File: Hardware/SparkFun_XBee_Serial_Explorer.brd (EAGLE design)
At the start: 57.1 x 48.3 mm, 51 parts, among them Q1 MBT2222, U1 MAX232SOIC16, U2 XBEE-1B3, U3 LM117

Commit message: Final QC checklist and changes for testbed
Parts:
- moved TP2 1.27 mm to (24.1, 16.5)
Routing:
- net RS232-CTS: track 24.8 -> 26.0 mm
- net RTS: track 42.0 -> 42.5 mm
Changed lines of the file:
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@@
 <layer number="47" name="Measures" color="7" fill="1" visible="no" active="yes"/>
 <layer number="48" name="Document" color="7" fill="1" visible="no" active="yes"/>
-<layer number="49" name="Reference" color="7" fill="1" visible="yes" active="yes"/>
+<layer number="49" name="Reference" color="7" fill="1" visible="no" active="yes"/>
 <layer number="50" name="dxf" color="7" fill="1" visible="no" active="yes"/>
 <layer number="51" name="tDocu" color="6" fill="1" visible="yes" active="yes"/>
@@
 <element name="LOGO3" library="SparkFun-Aesthetics" package="SFE_LOGO_FLAME_.1" value="SFE_LOGO_FLAME.1_INCH" x="6.604" y="1.3208"/>
 <element name="TP1" library="SparkFun-Passives" package="TP_15TH" value="TEST-POINTTP_15TH_THRU" x="25.4" y="19.05"/>
-<element name="TP2" library="SparkFun-Passives" package="TP_15TH" value="TEST-POINTTP_15TH_THRU" x="24.13" y="17.78"/>
+<element name="TP2" library="SparkFun-Passives" package="TP_15TH" value="TEST-POINTTP_15TH_THRU" x="24.13" y="16.51"/>
 <element name="TP3" library="SparkFun-Passives" package="TP_15TH" value="TEST-POINTTP_15TH_THRU" x="8.89" y="34.29"/>
 <element name="TP4" library="SparkFun-Passives" package="TP_15TH" value="TEST-POINTTP_15TH_THRU" x="21.59" y="34.29"/>
@@
 <wire x1="10.82" y1="15.94" x2="6.92" y2="15.94" width="0.254" layer="1"/>
 <wire x1="6.92" y1="15.94" x2="5.08" y2="17.78" width="0.254" layer="1"/>
-<wire x1="26.67" y1="15.875" x2="6.985" y2="15.875" width="0.254" layer="16"/>
-<wire x1="6.985" y1="15.875" x2="5.08" y2="17.78" width="0.254" layer="16"/>
+<wire x1="7.62" y1="15.24" x2="5.08" y2="17.78" width="0.254" layer="16"/>
 <wire x1="27.051" y1="16.256" x2="26.67" y2="15.875" width="0.254" layer="1"/>
+<wire x1="7.62" y1="15.24" x2="26.035" y2="15.24" width="0.254" layer="16"/>
+<wire x1="26.035" y1="15.24" x2="26.67" y2="15.875" width="0.254" layer="16"/>
 </signal>
 <signal name="DIO3">
@@
 <wire x1="24.765" y1="22.6" x2="24.765" y2="20.32" width="0.254" layer="1"/>
 <wire x1="24.765" y1="20.32" x2="24.13" y2="19.685" width="0.254" layer="1"/>
-<wire x1="24.13" y1="19.685" x2="24.13" y2="17.78" width="0.254" layer="1"/>
+<wire x1="24.13" y1="19.685" x2="24.13" y2="16.51" width="0.254" layer="1"/>
 </signal>
 <signal name="RS232-DTR">

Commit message: moved fids slightly
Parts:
- moved U$16 2.84 mm to (54.6, 7.62)
- moved U$7 2.84 mm to (2.54, 40.6)

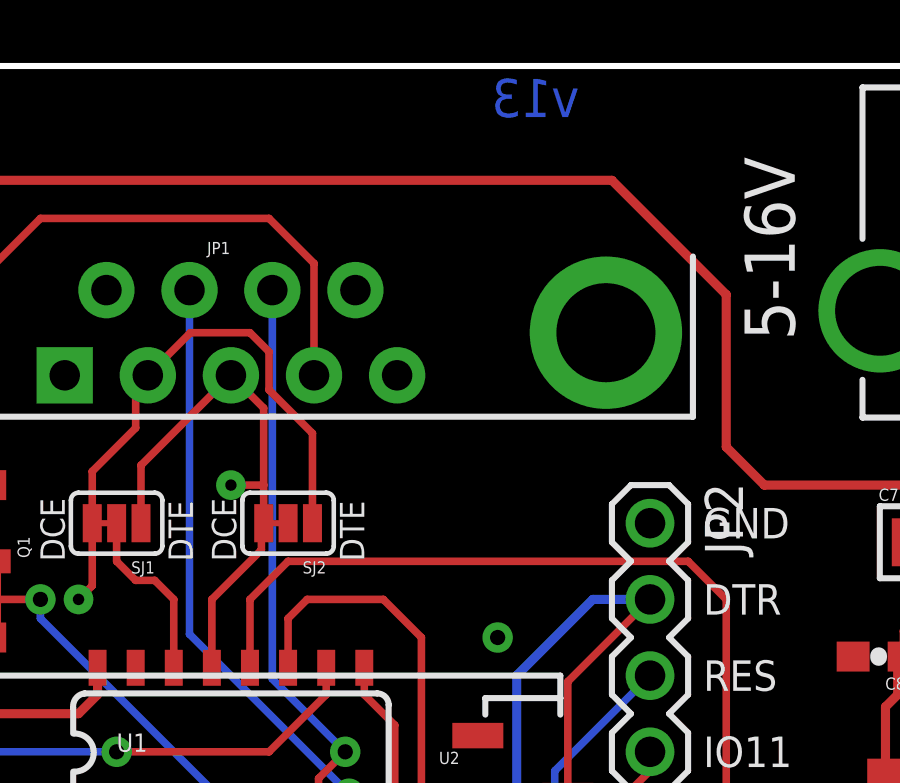
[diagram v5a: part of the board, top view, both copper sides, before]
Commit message: Fixing jumper trace, updating version number
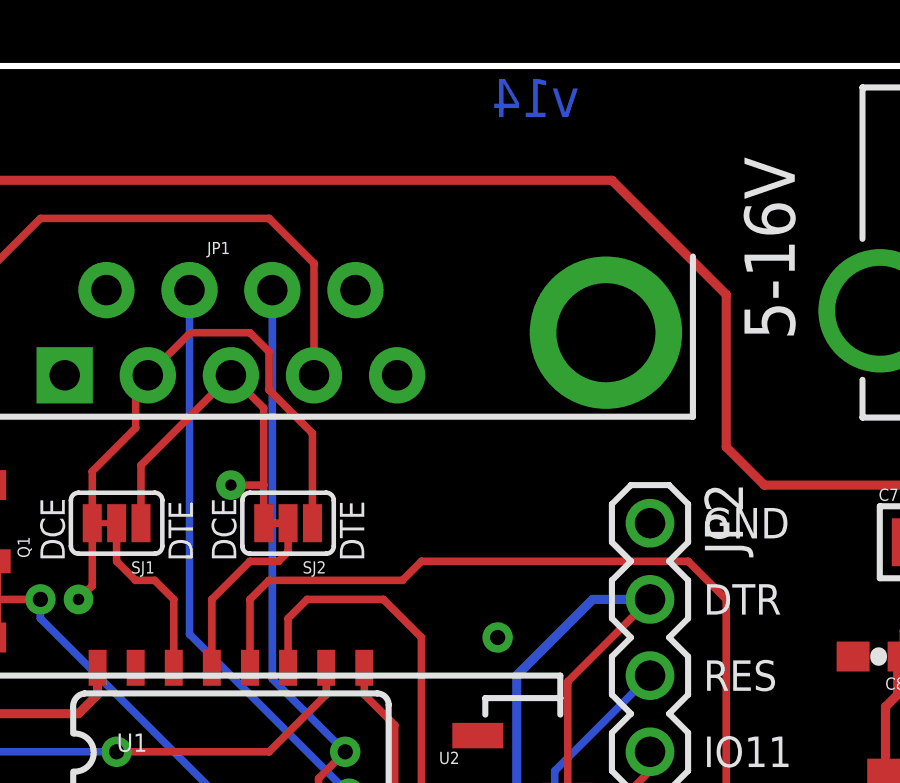
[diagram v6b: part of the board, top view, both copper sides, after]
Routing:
- net N$13: track 5.61 -> 7.07 mm
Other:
- board text added: "v14"
- board text removed: "v13"
